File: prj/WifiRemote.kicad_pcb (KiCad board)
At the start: 2 copper layers, 40 x 75 mm, 68 parts, among them J1 DIP-BLACK-MALE-HEADER-VERT_4P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, J2 DIP-BLACK-MALE-HEADER_6P-2.54_, K1 DIP-SWITCH-TACTILE-SPST-NO_TS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, K2 DIP-SWITCH-TACTILE-SPST-NO_TS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, K3 DIP-SWITCH-TACTILE-SPST-NO_TS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, K4 DIP-SWITCH-TACTILE-SPST-NO_TS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, M1 Mechanical_Mount, M2 Mechanical_Mount, M3 Mechanical_Mount, M4 Mechanical_Mount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

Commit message: Swapped D2 and D3
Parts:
- moved D3 5.12 mm to (87.0, 94.9)
- moved D2 4.96 mm to (87.0, 100.0)
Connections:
- R7 pad 1: Net-(D2-Pad-) -> Net-(D3-Pad-)
- R8 pad 1: Net-(D3-Pad-) -> Net-(D2-Pad-)
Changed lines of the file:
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@@
   (general
     (links 129)
-    (no_connects 0)
-    (area 39.371833 61.722499 102.152167 165.6432)
+    (no_connects 2)
+    (area 49.949999 74.949999 90.050001 150.050001)
     (thickness 1.6)
     (drawings 4)
-    (tracks 471)
+    (tracks 470)
     (zones 0)
     (modules 68)
@@
   )
   (module SeeedOPL-LED-2016:LED-0805 (layer F.Cu)
-    (at 87 100)
+    (at 87 94.882)
     (attr smd)
     (fp_text reference D3 (at 2.3192 -0.038 90) (layer F.SilkS)
@@
     (fp_line (start -0.635 -1.397) (end 0.635 -1.397) (layer F.SilkS) (width 0.127))
     (pad 1 smd rect (at 0 -0.762 180) (size 0.889 0.889) (layers F.Cu F.Paste F.Mask)
-      (net 36 "Net-(D2-Pad-)"))
+      (net 9 "Net-(D3-Pad-)"))
     (pad 2 smd rect (at 0 0.762 180) (size 0.889 0.889) (layers F.Cu F.Paste F.Mask)
       (net 19 FTDI_RXI))
@@
     (fp_line (start -0.635 -1.397) (end 0.635 -1.397) (layer F.SilkS) (width 0.127))
     (pad 1 smd rect (at 0 -0.762 180) (size 0.889 0.889) (layers F.Cu F.Paste F.Mask)
-      (net 9 "Net-(D3-Pad-)"))
+      (net 36 "Net-(D2-Pad-)"))
     (pad 2 smd rect (at 0 0.762 180) (size 0.889 0.889) (layers F.Cu F.Paste F.Mask)
       (net 26 GPIO2))
@@
   )
   (module SeeedOPL-LED-2016:LED-0805 (layer F.Cu)
-    (at 87 95)
+    (at 86.957 99.962)
     (attr smd)
     (fp_text reference D2 (at 2.2684 0.0598 90) (layer F.SilkS)
@@
   (segment (start 87.889 90) (end 87.889 91.873) (width 0.2) (layer F.Cu) (net 7))
   (segment (start 87.889 91.873) (end 87.762 92) (width 0.2) (layer F.Cu) (net 7))
+  (segment (start 87 91) (end 87 93.866) (width 0.2) (layer F.Cu) (net 8))
+  (segment (start 86.154 94.712) (end 87 93.866) (width 0.2) (layer F.Cu) (net 8))
+  (segment (start 86.111 94.882) (end 86.111 94.712) (width 0.25) (layer F.Cu) (net 8))
   (segment (start 59.5 104.25) (end 66.75 97) (width 0.6) (layer B.Cu) (net 8))
   (segment (start 66.75 97) (end 84.75 97) (width 0.6) (layer B.Cu) (net 8))
@@
   (segment (start 56.7555 77.099) (end 56.6485 77.099) (width 0.2) (layer F.Cu) (net 8))
   (segment (start 56.6485 77.099) (end 55.75 77.099) (width 0.2) (layer F.Cu) (net 8))
-  (segment (start 87 94) (end 86.982501 94.017499) (width 0.2) (layer F.Cu) (net 8))
   (segment (start 86.111 90) (end 86.111 90.111) (width 0.2) (layer F.Cu) (net 8))
   (segment (start 86.111 94.8095) (end 86.111 95) (width 0.2) (layer F.Cu) (net 8))
   (segment (start 86.111 90.111) (end 87 91) (width 0.2) (layer F.Cu) (net 8))
-  (segment (start 87 91) (end 87 94) (width 0.2) (layer F.Cu) (net 8))
-  (segment (start 87 94) (end 86.9205 94) (width 0.2) (layer F.Cu) (net 8))
-  (segment (start 86.9205 94) (end 86.111 94.8095) (width 0.2) (layer F.Cu) (net 8))
   (segment (start 83.25 90) (end 82.262 90.988) (width 0.2) (layer F.Cu) (net 8))
   (segment (start 82.262 90.988) (end 82.262 92) (width 0.2) (layer F.Cu) (net 8))
@@
   (segment (start 82.262 94) (end 82.262 93.3555) (width 0.2) (layer F.Cu) (net 8))
   (segment (start 82.262 93.3555) (end 82.262 92) (width 0.2) (layer F.Cu) (net 8))
-  (segment (start 87.889 100) (end 87.889 101.873) (width 0.3) (layer F.Cu) (net 9))
-  (segment (start 87.889 101.873) (end 87.762 102) (width 0.3) (layer F.Cu) (net 9))
+  (segment (start 87.889 95) (end 87.889 96.873) (width 0.2) (layer F.Cu) (net 9))
+  (segment (start 87.889 96.873) (end 87.762 97) (width 0.2) (layer F.Cu) (net 9))
   (segment (start 76 90) (end 78 90) (width 0.3) (layer F.Cu) (net 10))
   (segment (start 85.8 132.8) (end 87.95 132.8) (width 0.3) (layer F.Cu) (net 10))
@@
   (segment (start 58.75 131.0052) (end 58.75 131.75) (width 0.254) (layer F.Cu) (net 28))
   (via (at 58.75 131.75) (size 0.6) (drill 0.4) (layers F.Cu B.Cu) (net 28))
-  (segment (start 87.889 95) (end 87.889 96.873) (width 0.2) (layer F.Cu) (net 36))
-  (segment (start 87.889 96.873) (end 87.762 97) (width 0.2) (layer F.Cu) (net 36))
+  (segment (start 87.889 100) (end 87.889 101.873) (width 0.3) (layer F.Cu) (net 36))
+  (segment (start 87.889 101.873) (end 87.762 102) (width 0.3) (layer F.Cu) (net 36))
   (segment (start 84.151 88) (end 85.0495 88) (width 0.2) (layer F.Cu) (net 37))
   (segment (start 85.0495 88) (end 86.488 88) (width 0.2) (layer F.Cu) (net 37))

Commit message: changes stemming from layout review
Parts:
- D1: value SMD-LED-CLEAR-GREEN_0805_ -> SMD-LED-CLEAR-BLUE_0805_
- D2: value SMD-LED-CLEAR-BLUE_0805_ -> SMD-LED-CLEAR-GREEN_0805_
- J1: value DIP-BLACK-MALE-HEADER-VERT_4P-2.54_ -> 2AA_Battery; footprint SeeedOPL-Connector-2016:H4-2.54 -> ICEE-Connector:header_1x2
- moved R6 10.0 mm to (87.0, 102.0)
- moved D1 5.00 mm to (87.0, 95.0)
- moved R7 5.00 mm to (87.0, 92.0)
- moved R8 5.00 mm to (87.0, 97.0)
- moved D3 4.88 mm to (87.0, 90.0)
- moved M3 2.68 mm to (55.0, 140.0)
- moved M1 2.60 mm to (55.0, 110.0)
- moved M2 2.59 mm to (85.0, 110.0)
- moved M4 2.28 mm to (85.0, 140.0)
- moved D4 0.40 mm to (78.0, 141.0)
- moved Q1 0.40 mm to (73.6, 141.0)
- moved R13 0.40 mm to (76.4, 139.3)
- moved J2 0.34 mm to (52.0, 92.0)
- moved R1 0.30 mm to (58.5, 84.2)
- moved R10 0.30 mm to (58.5, 86.0)
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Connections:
- J1 pad 1: GNDD -> +BATT
- R6 pad 1: Net-(D1-Pad-) -> Net-(D2-Pad-)
- R8 pad 1: Net-(D2-Pad-) -> Net-(D1-Pad-)
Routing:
- net GNDD: track 360.5 -> 330.2 mm, vias 9 -> 58
- net GPIO13: track 122.9 -> 97.1 mm
- net FTDI_RXI: track 55.5 -> 43.5 mm
- net +BATT: track 108.4 -> 99.8 mm, vias 1 -> 0
- net GPIO2: track 19.0 -> 10.6 mm
- net GPIO12: track 46.9 -> 53.3 mm
- net FTDI_DTR: track 47.1 -> 41.1 mm
- net GPIO14: track 54.5 -> 57.3 mm
- net +3V3: track 124.7 -> 121.9 mm
- net GPIO5: track 60.4 -> 58.1 mm
- net GPIO4: track 60.6 -> 58.6 mm
- net Net-(Q1-Pad3): track 6.47 -> 8.10 mm
- net FTDI_TXO: track 34.0 -> 33.0 mm
- net GPIO0: track 38.2 -> 37.4 mm
- net /BTN_PWR: track 48.3 -> 47.5 mm
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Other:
- board text added: "-+"
- board text added: "NEXT"
- board text added: "ON<>OFF"
- board text added: "PREV"
- board text added: "START"
- board text added: "STOP/RST"

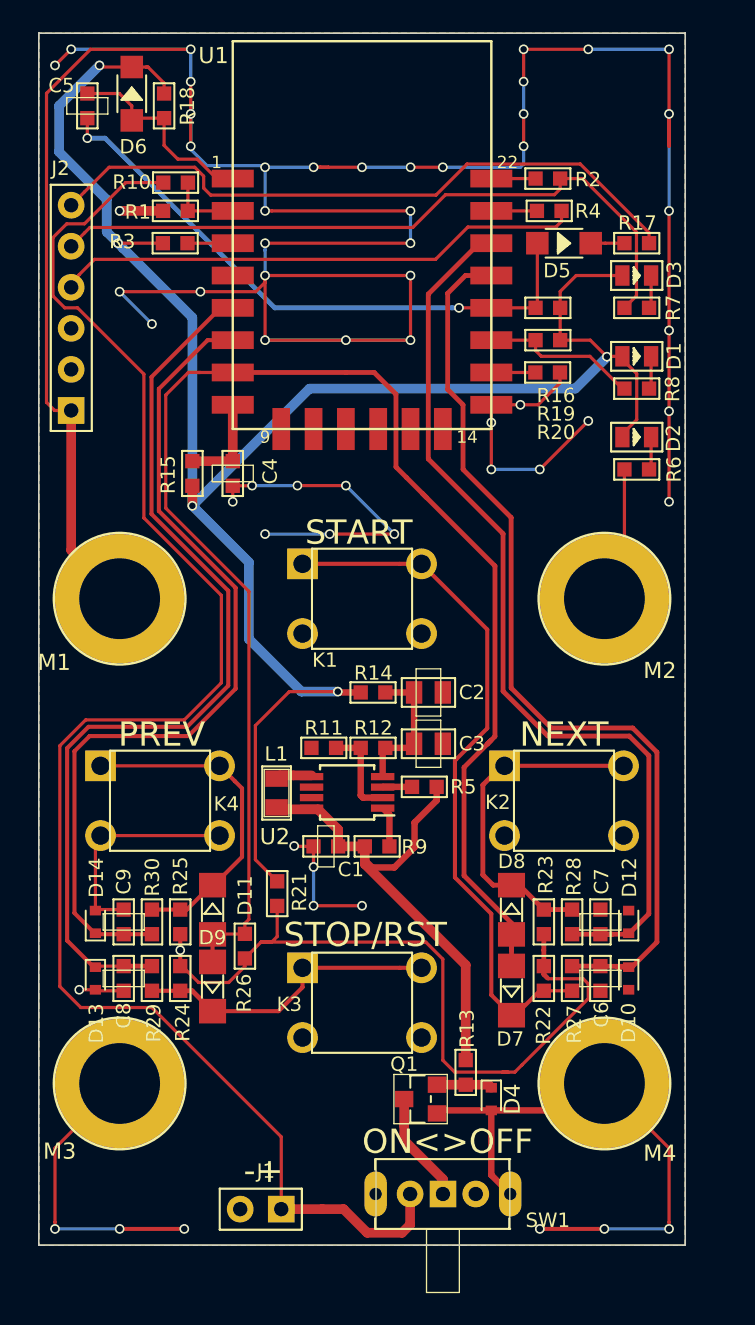
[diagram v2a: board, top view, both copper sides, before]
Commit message: Updates to diodes
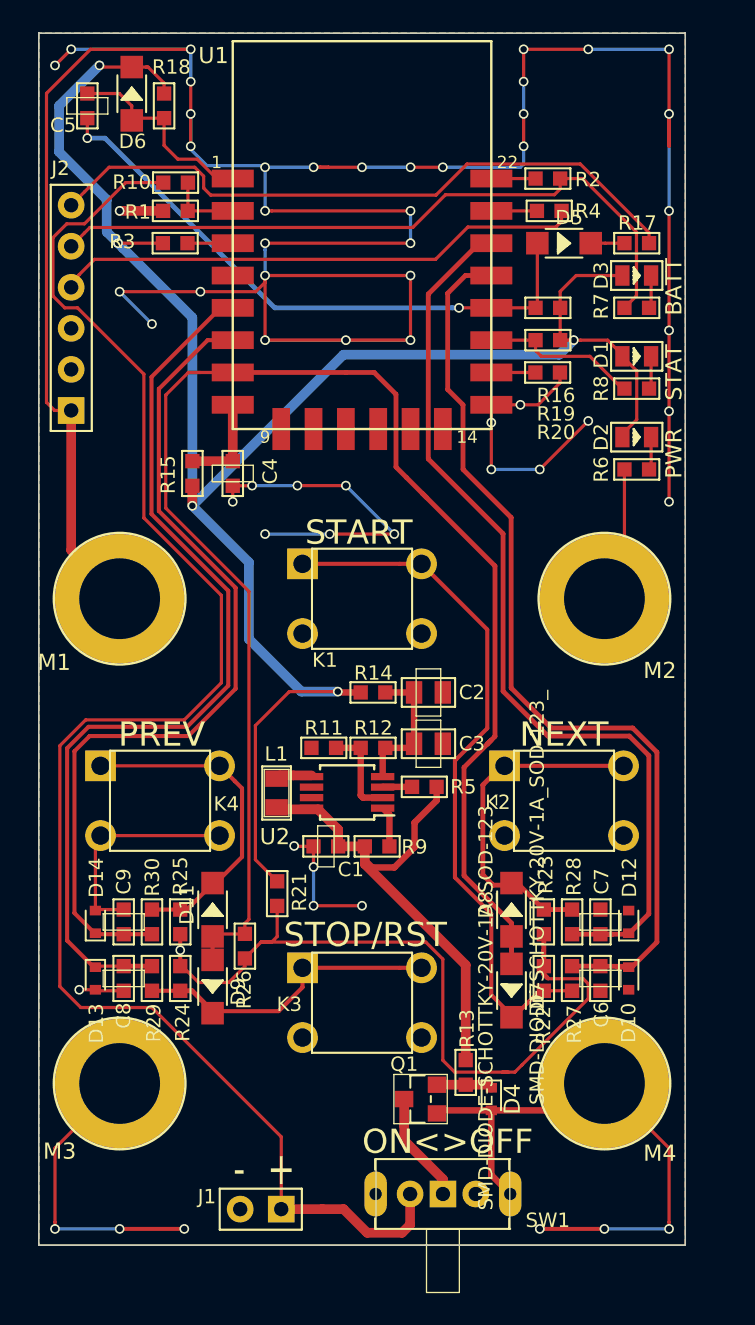
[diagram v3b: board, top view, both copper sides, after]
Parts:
- D11, D7, D8, D9: value SMD-DIODE-SWITCH-1N4148_LL-34_ -> SMD-DIODE-SCHOTTKY-20V-1A_SOD-123_; footprint SeeedOPL-Diode-2016:LL-34 -> SeeedOPL-Diode-2016:SOD-123
- D5, D6: value SMD-DIODE-SCHOTTKY-20V-500MA_SOD-123_ -> SMD-DIODE-SCHOTTKY-20V-1A_SOD-123_
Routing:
- net +3V3: track 121.9 -> 120.3 mm
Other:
- board text added: "+"
- board text added: "-"
- board text added: "BATT"
- board text added: "PWR"
- board text added: "STAT"
- board text removed: "-+"

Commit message: Changed LED annotations
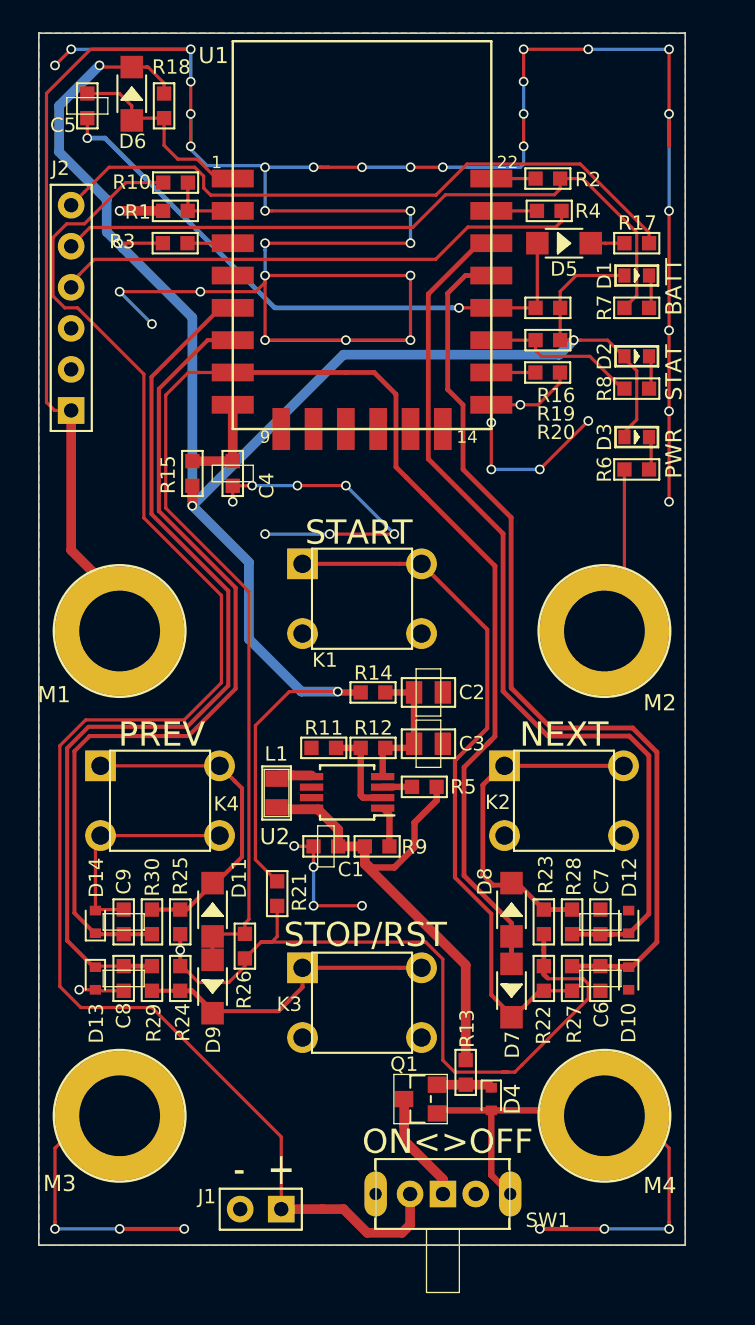
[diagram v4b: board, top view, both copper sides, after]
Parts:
- D1: value SMD-LED-CLEAR-BLUE_0805_ -> LED-SMD-RED-DIFFUSED_0603_; footprint SeeedOPL-LED-2016:LED-0805 -> SeeedOPL-LED-2016:LED-0603
- D2: value SMD-LED-CLEAR-GREEN_0805_ -> SMD-LED-CLEAR-BLUE_0603_; footprint SeeedOPL-LED-2016:LED-0805 -> SeeedOPL-LED-2016:LED-0603
- D3: value SMD-LED-CLEAR-RED_0805_ -> SMD-LED-CLEAR-GREEN_0603_; footprint SeeedOPL-LED-2016:LED-0805 -> SeeedOPL-LED-2016:LED-0603
- moved D3 10.0 mm to (87.0, 100.0)
- moved D1 5.00 mm to (87.0, 90.0)
- moved D2 5.00 mm to (87.0, 95.0)
- moved M1 2.00 mm to (55.0, 112.0)
- moved M2 2.00 mm to (85.0, 112.0)
- moved M3 2.00 mm to (55.0, 142.0)
- moved M4 2.00 mm to (85.0, 142.0)
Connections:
- R6 pad 1: Net-(D2-Pad-) -> Net-(D3-Pad-)
- R7 pad 1: Net-(D3-Pad-) -> Net-(D1-Pad-)
- R8 pad 1: Net-(D1-Pad-) -> Net-(D2-Pad-)

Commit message: Added silkscreen logos
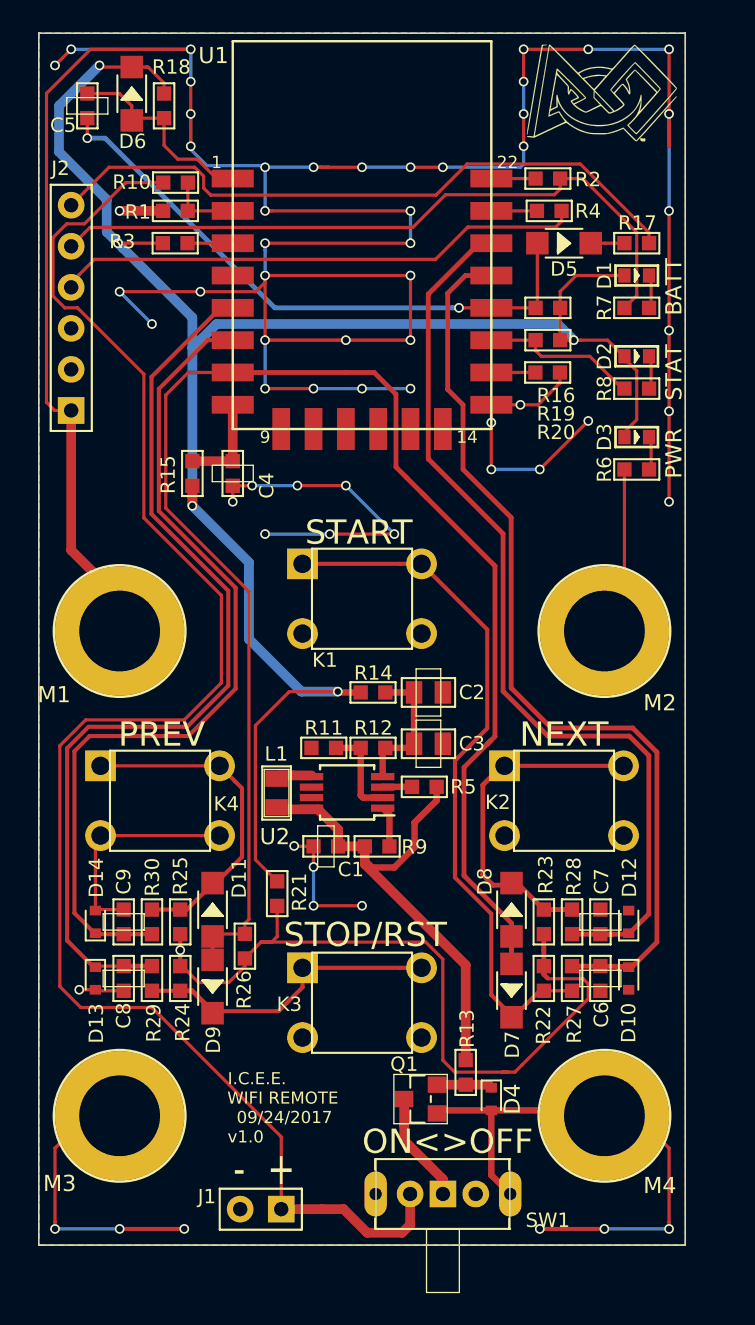
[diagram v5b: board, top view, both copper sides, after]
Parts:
- added G***: LOGO, ICEE-Logos:FTC_Logo_Outline_BW_Large, B.Cu at (69.1, 110.6)
- added G***: LOGO, ICEE-Logos:FTC_Logo_Outline_BW_0R5IN, F.Cu at (84.8, 78.7)
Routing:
- net GNDD: track 330.2 -> 342.2 mm, vias 58 -> 62
- net +3V3: track 120.3 -> 117.1 mm
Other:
- board text added: "09/24/2017"
- board text added: "I.C.E.E."
- board text added: "WIFI REMOTE"
- board text added: "v1.0"
